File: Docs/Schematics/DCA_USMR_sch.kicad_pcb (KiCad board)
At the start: 4 copper layers, 54 parts, among them J1 Conn_02x03_Counter_Clockwise, J2 RJ45, J3 Barrel_Jack_Switch, U1 SAMD20, U2 LD1117S33TR_SOT223, U3 ATWINC1500-MR, U4 ENC28J60, Y1 25MHz

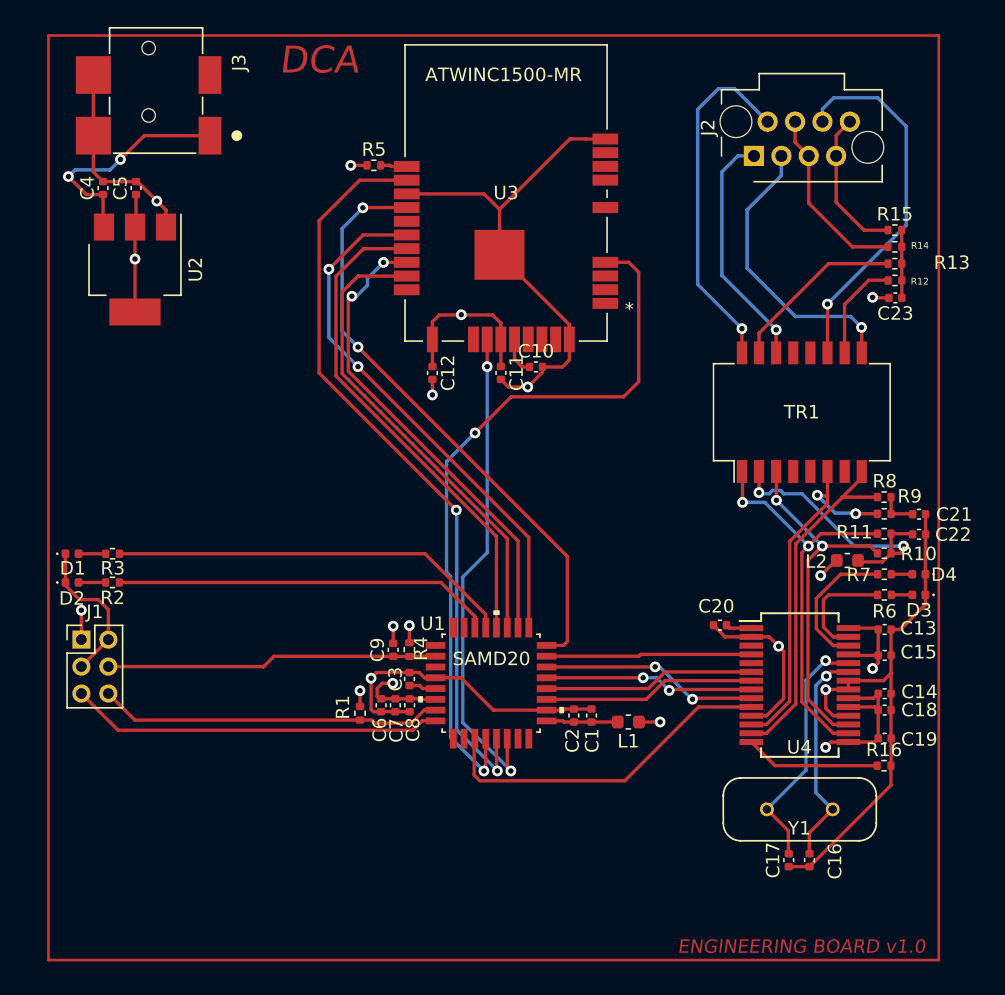
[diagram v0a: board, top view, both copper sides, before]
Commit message: Revision v1.1
Main PCB changes, Moved power to bottom right. Made power rails 0.5mil.
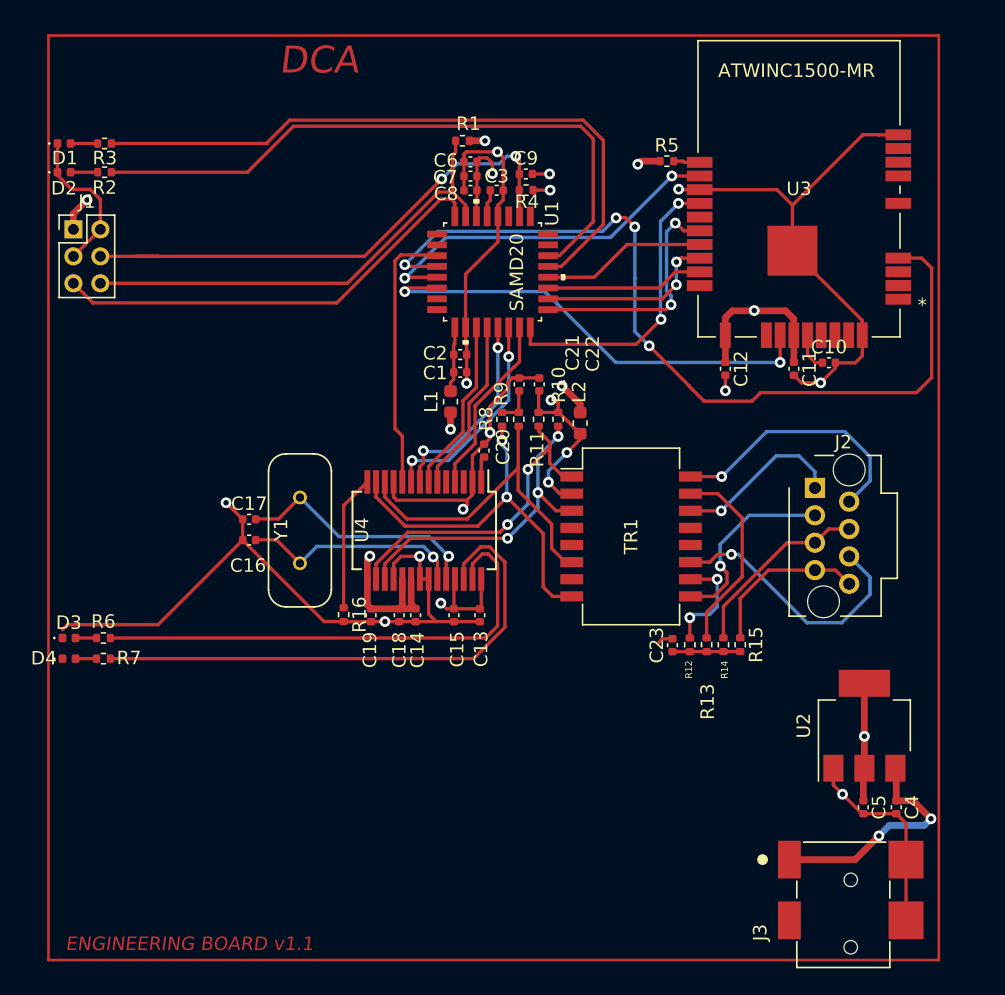
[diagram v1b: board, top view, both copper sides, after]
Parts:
- moved C4 74.6 mm to (263.8, 149.5), turned to -90 degrees
- moved C5 70.8 mm to (261.3, 149.5), turned to -90 degrees
- moved J3 68.8 mm to (255.8, 153.4), turned to 90 degrees
- moved U2 63.8 mm to (261.4, 143.4), turned to 90 degrees
- moved D4 63.3 mm to (202.4, 138.5), turned to 0 degrees
- moved D3 63.1 mm to (202.4, 136.9), turned to 0 degrees
- moved R7 58.3 mm to (205.0, 138.5), turned to 0 degrees
- moved R6 58.0 mm to (205.0, 136.9), turned to 180 degrees
- moved C16 47.9 mm to (215.8, 129.7), turned to 0 degrees
- moved C17 47.3 mm to (215.8, 128.1), turned to 0 degrees
- moved R1 43.1 mm to (231.6, 100.0), turned to 180 degrees
- moved Y1 42.5 mm to (219.5, 128.9), turned to -90 degrees
- moved R16 41.6 mm to (222.8, 135.2), turned to -90 degrees
- moved C6 40.9 mm to (232.2, 101.6), turned to 180 degrees
- moved C7 39.6 mm to (232.2, 102.7), turned to 180 degrees
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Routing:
- net GND: track 280.8 -> 216.9 mm, vias 8 -> 12
- net Net-(R7-Pad2): track 10.4 -> 40.2 mm
- net WINC_WAKE: track 56.5 -> 27.4 mm
- net Net-(R6-Pad1): track 8.33 -> 37.3 mm
- net WINC_SS: track 37.1 -> 12.4 mm
- net WINC_SCK: track 35.3 -> 11.8 mm
- net WINC_EXTINT: track 44.6 -> 22.5 mm
- net WINC_MISO: track 35.3 -> 13.5 mm
- net WINC_MOSI: track 39.6 -> 17.8 mm
- net Net-(R2-Pad2): track 28.2 -> 48.1 mm
- net Net-(R3-Pad2): track 30.0 -> 49.5 mm
- net Net-(C9-Pad1): track 24.6 -> 40.1 mm, vias 0 -> 2
- net WINC_RESET: track 54.2 -> 64.8 mm, vias 2 -> 4
- net Net-(J1-Pad6): track 25.6 -> 35.0 mm
- net Net-(C22-Pad1): track 21.3 -> 13.3 mm, vias 2 -> 3
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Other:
- board text added: "ENGINEERING BOARD v1.1"
- board text removed: "ENGINEERING BOARD v1.0"
